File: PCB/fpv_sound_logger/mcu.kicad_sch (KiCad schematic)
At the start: 21 parts, among them IC1 W25Q128JVSIQ, U4 SC0914_13_, Y1 ABM8-272-T3

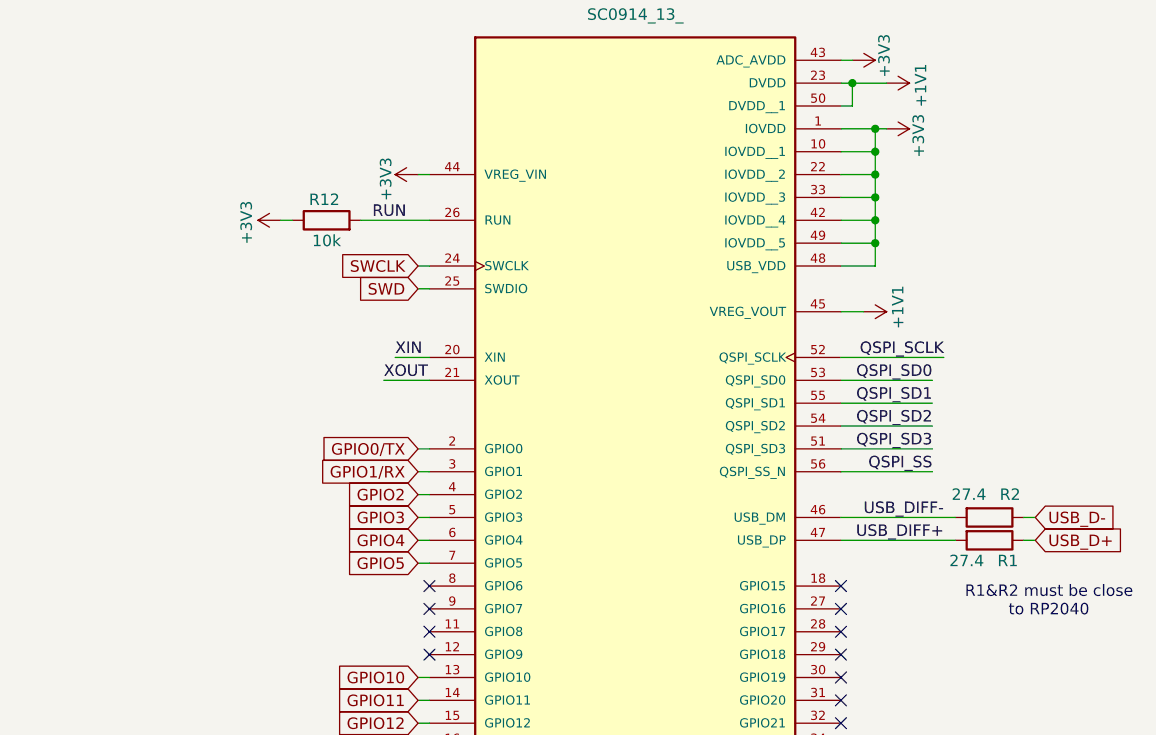
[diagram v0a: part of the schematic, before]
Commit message: place new components and started routing for v2
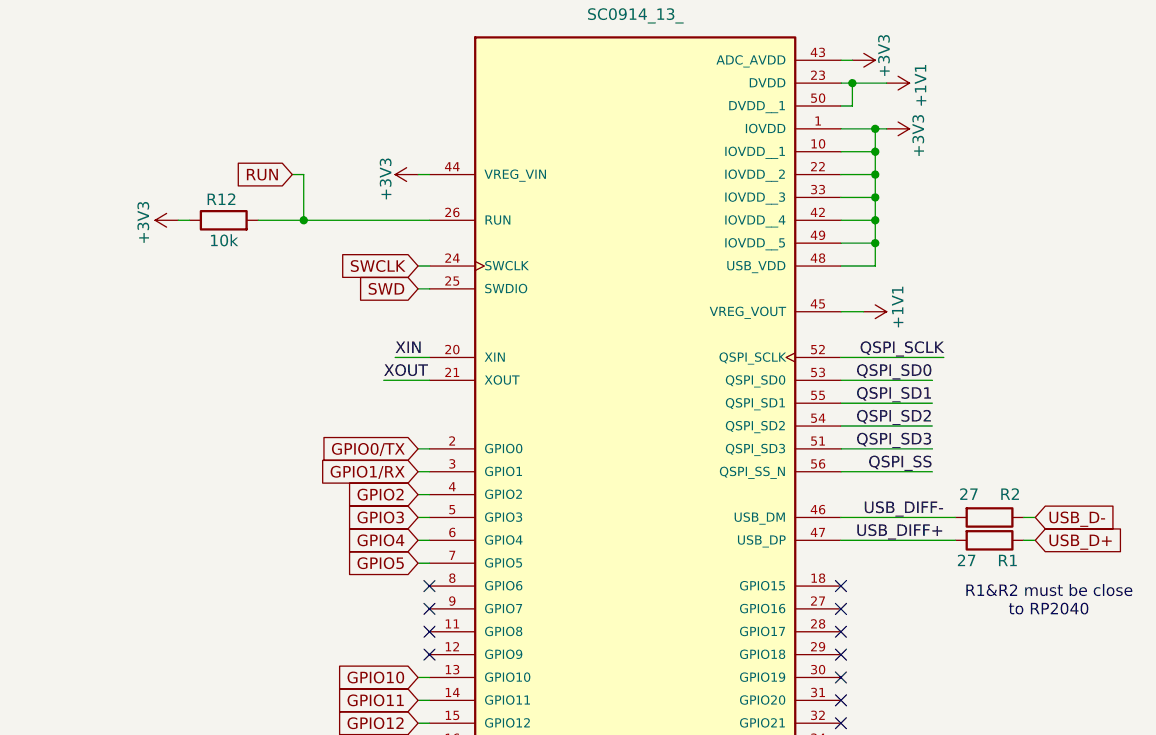
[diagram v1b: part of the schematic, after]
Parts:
- IC1: Manufacturer Winbond -> (none)
- R1, R2: value 27.4 -> 27; footprint Capacitor_SMD:C_0805_2012Metric -> Resistor_SMD:R_0805_2012Metric
- R12, R3: footprint Capacitor_SMD:C_0805_2012Metric -> Resistor_SMD:R_0805_2012Metric
- Y1: Manufacturer ABRACON -> (none)
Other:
- moved on the sheet: R12

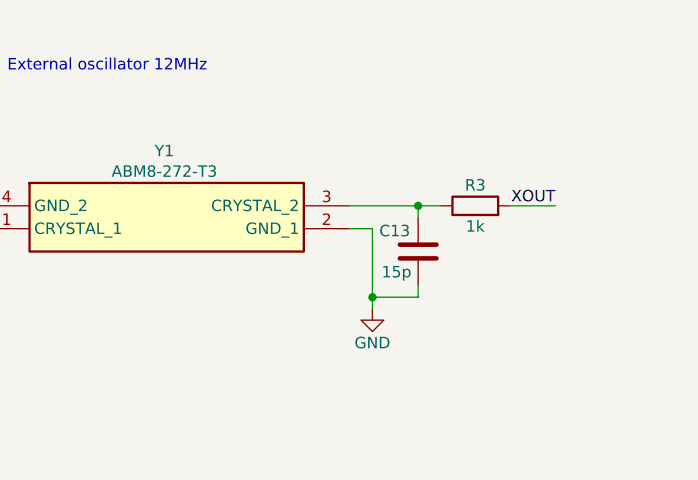
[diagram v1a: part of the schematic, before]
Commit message: Update component footprints and add manufacturer details in sensor schematic
- Changed resistor footprint from R_0805 to R_0603 for multiple components.
- Updated manufacturer part numbers, manufacturers, suppliers, and supplier parts for various components.
- Added manufacturer and supplier information for OMRON components.
- Removed outdated datasheet link and replaced with relevant part numbers for clarity.
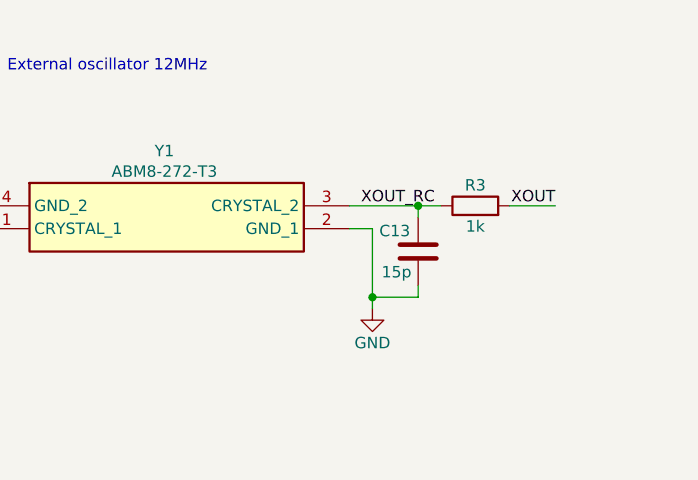
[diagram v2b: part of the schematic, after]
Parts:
- C1, C10, C11, C14, C2, C3, C4, C5, C6, C7: footprint Capacitor_SMD:C_0805_2012Metric -> Capacitor_SMD:C_0603_1608Metric; MANUFACTURER (none) -> Samsung Electro-Mechanics; Manufacturer_Part_Number (none) -> CL10B104KB8NNNC; Supplier (none) -> LCSC; Supplier Part (none) -> C1591
- C12, C13: footprint Capacitor_SMD:C_0805_2012Metric -> Capacitor_SMD:C_0603_1608Metric; MANUFACTURER (none) -> Samsung Electro-Mechanics; Manufacturer_Part_Number (none) -> CL10C150JB8NNNC; Supplier (none) -> LCSC; Supplier Part (none) -> C1644
- C8, C9: footprint Capacitor_SMD:C_0805_2012Metric -> Capacitor_SMD:C_0603_1608Metric; MANUFACTURER (none) -> Samsung Electro-Mechanics; Manufacturer_Part_Number (none) -> CL10B105KA8NNNC; Supplier (none) -> LCSC; Supplier Part (none) -> C29936
- R1, R2: footprint Resistor_SMD:R_0805_2012Metric -> Resistor_SMD:R_0603_1608Metric; MANUFACTURER (none) -> PANASONIC; Manufacturer_Part_Number (none) -> ERJ3EKF27R0V; Supplier (none) -> LCSC; Supplier Part (none) -> C403127
- R12: footprint Resistor_SMD:R_0805_2012Metric -> Resistor_SMD:R_0603_1608Metric; MANUFACTURER (none) -> PANASONIC; Manufacturer_Part_Number (none) -> ERJUP3F1002V; Supplier (none) -> LCSC; Supplier Part (none) -> ERJUP3F1002V
- R3: footprint Resistor_SMD:R_0805_2012Metric -> Resistor_SMD:R_0603_1608Metric; MANUFACTURER (none) -> PANASONIC; Manufacturer_Part_Number (none) -> ERJ3EKF1001V; Supplier (none) -> LCSC; Supplier Part (none) -> C118155
- U4: Manufacturer_Part_Number (none) -> SC0914(13); Supplier (none) -> LCSC; Supplier Part (none) -> C3227924
- Y1: MANUFACTURER (none) -> ABRACON; Supplier (none) -> LCSC; Supplier Part (none) -> C20625731
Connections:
- net XOUT_RC: now reaches C13.1, R3.1, Y1.3 (CRYSTAL_2)

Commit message: Refactor code structure for improved readability and maintainability
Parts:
- IC1: MANUFACTURER (none) -> Winbond; Supplier (none) -> LCSC; Supplier Part (none) -> C113767
- U4: Manufacturer_Part_Number SC0914(13) -> RP2040; Supplier Part C3227924 -> C2040
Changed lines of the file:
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@@
+			)
+		)
+		(property "MANUFACTURER" "Winbond"
+			(at 35.56 34.29 0)
+			(hide yes)
+			(show_name no)
+			(do_not_autoplace no)
+			(effects
+				(font
+					(size 1.27 1.27)
+				)
+			)
+		)
+		(property "Supplier" "LCSC"
+			(at 35.56 34.29 0)
+			(hide yes)
+			(show_name no)
+			(do_not_autoplace no)
+			(effects
+				(font
+					(size 1.27 1.27)
+				)
+			)
+		)
+		(property "Supplier Part" "C113767"
+			(at 35.56 34.29 0)
+			(hide yes)
+			(show_name no)
+			(do_not_autoplace no)
+			(effects
+				(font
+					(size 1.27 1.27)
+				)
 			)
 		)
@@
 			)
 		)
-		(property "Manufacturer_Part_Number" "SC0914(13)"
+		(property "Manufacturer_Part_Number" "RP2040"
 			(at 95.25 118.11 0)
 			(hide yes)
@@
 			)
 		)
-		(property "Supplier Part" "C3227924"
+		(property "Supplier Part" "C2040"
 			(at 95.25 118.11 0)
 			(hide yes)
